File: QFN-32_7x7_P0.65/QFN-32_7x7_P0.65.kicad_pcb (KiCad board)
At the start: 2 copper layers, 25.4 x 45.7 mm, 6 parts, among them J101 Conn_01x26, J102 Conn_01x26, J103 Conn_01x26, J104 Conn_01x26, U101 QFN-48

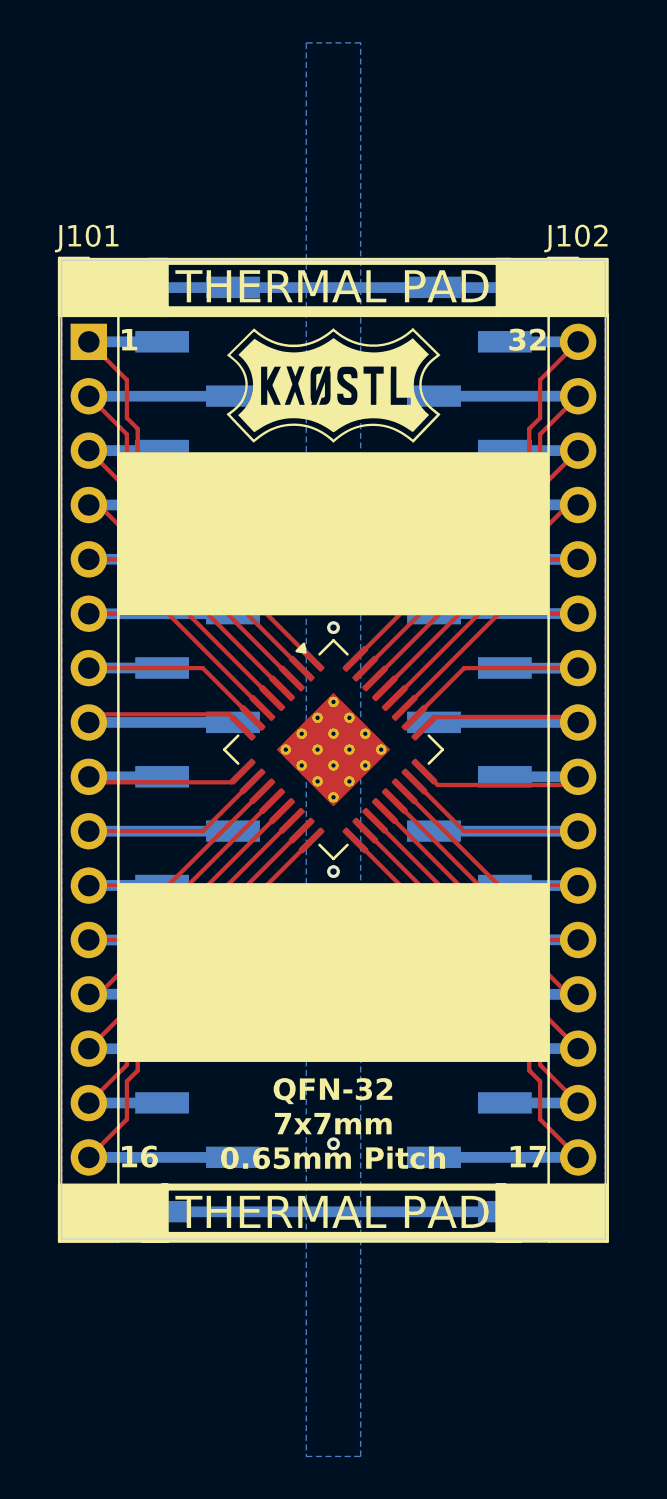
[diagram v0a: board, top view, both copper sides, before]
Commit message: Created SMDIP-16, QFP-48, QFP-32, QFN-80, QFN-68, QFN-64, QFN-60, QFN-56, QFN-48, QFN-36, QFN-28, QFN-20, QFP-32, QFP-48
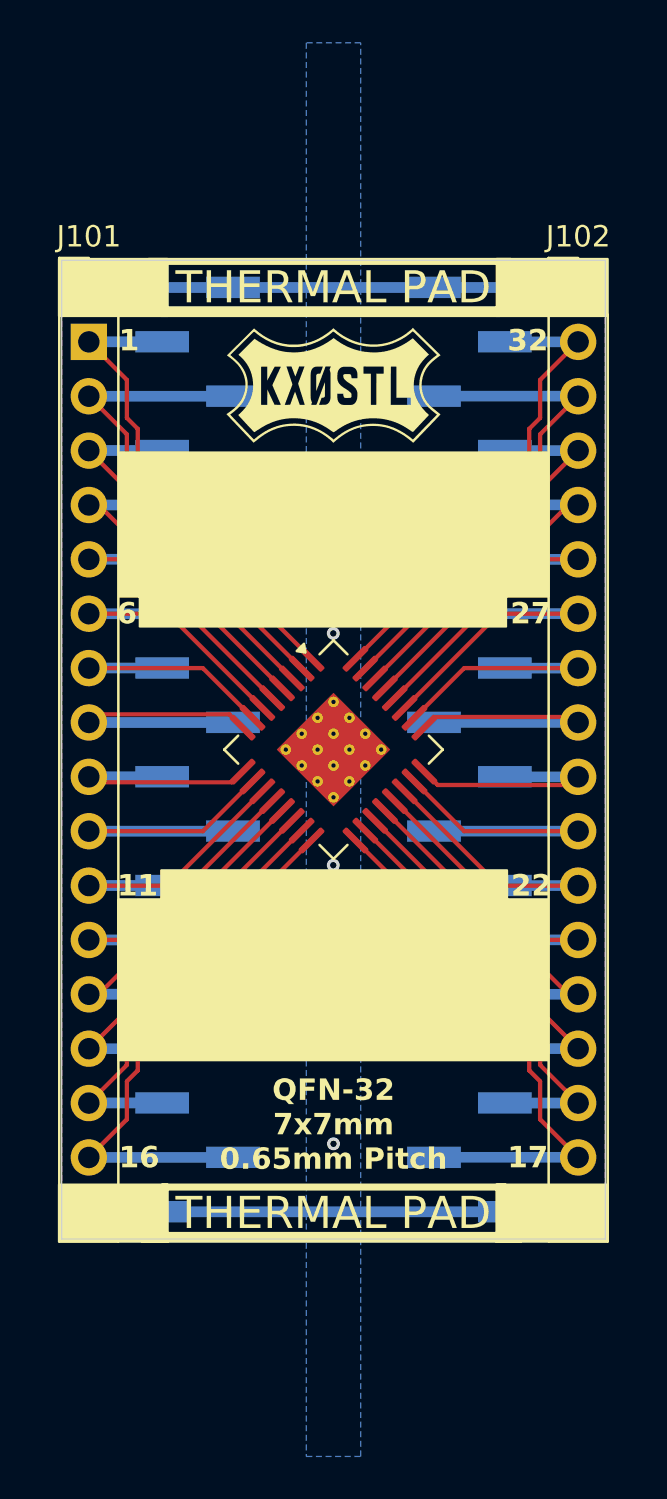
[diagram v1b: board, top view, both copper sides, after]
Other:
- board text added: "11"
- board text added: "22"
- board text added: "27"
- board text added: "6"
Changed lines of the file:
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@@
+	)
+	(gr_rect
+		(start 129.377 108.1456)
+		(end 146.493 114.9)
+		(stroke
+			(width 0.1)
+			(type solid)
+		)
+		(fill yes)
+		(layer "F.SilkS")
 	)
 	(gr_rect
@@
 	)
 	(gr_rect
+		(start 130.382 126.2856)
+		(end 146.538 128.89)
+		(stroke
+			(width 0.1)
+			(type solid)
+		)
+		(fill yes)
+		(layer "F.SilkS")
+	)
+	(gr_rect
 		(start 129.7855 97.726375)
 		(end 146.72725 97.954975)
+		(stroke
+			(width 0.1)
+			(type solid)
+		)
+		(fill yes)
+		(layer "F.SilkS")
+	)
+	(gr_rect
+		(start 128.374 127.66)
+		(end 148.43 134.271)
 		(stroke
 			(width 0.1)
@@
 	)
 	(gr_rect
-		(start 128.36935 106.807)
-		(end 148.43535 114.3254)
-		(stroke
-			(width 0.1)
-			(type solid)
-		)
-		(fill yes)
-		(layer "F.SilkS")
-	)
-	(gr_rect
 		(start 129.48075 143.2306)
 		(end 147.1845 143.637)
@@
 	)
 	(gr_rect
-		(start 128.397 126.9365)
-		(end 148.463 135.1915)
+		(start 125.603 97.726375)
+		(end 130.683 100.393625)
 		(stroke
 			(width 0.1)
@@
 	)
 	(gr_rect
-		(start 125.603 97.726375)
-		(end 130.683 100.393625)
+		(start 128.374 127.66)
+		(end 148.44 135.161)
+		(stroke
+			(width 0.1)
+			(type solid)
+		)
+		(fill yes)
+		(layer "F.SilkS")
+	)
+	(gr_rect
+		(start 128.40935 106.767)
+		(end 148.47535 113.5014)
 		(stroke
 			(width 0.1)
@@
 		)
 	)
+	(gr_text "22"
+		(at 148.63 127 0)
+		(layer "F.SilkS" knockout)
+		(effects
+			(font
+				(size 1 1)
+				(thickness 0.2)
+				(bold yes)
+			)
+			(justify right)
+		)
+	)
 	(gr_text "17"
 		(at 148.463 139.7 0)
 		(layer "F.SilkS")
+		(effects
+			(font
+				(size 1 1)
+				(thickness 0.2)
+				(bold yes)
+			)
+			(justify right)
+		)
+	)
+	(gr_text "27"
+		(at 148.6 114.29 0)
+		(layer "F.SilkS" knockout)
 		(effects
 			(font
@@
 		)
 	)
+	(gr_text "11"
+		(at 128.32 127 0)
+		(layer "F.SilkS" knockout)
+		(effects
+			(font
+				(size 1 1)
+				(thickness 0.2)
+				(bold yes)
+			)
+			(justify left)
+		)
+	)
 	(gr_text "THERMAL PAD"
 		(at 138.4215 99.06 0)
@@
 		)
 	)
-	(gr_text "1"
-		(at 128.397 101.536375 0)
-		(layer "F.SilkS")
+	(gr_text "6"
+		(at 128.3 114.29 0)
+		(layer "F.SilkS" knockout)
 		(effects
 			(font
@@
 		)
 	)
-	(gr_text "16"
-		(at 128.397 139.7 0)
+	(gr_text "1"
+		(at 128.397 101.536375 0)
 		(layer "F.SilkS")
 		(effects
@@
 		)
 	)
+	(gr_text "16"
+		(at 128.397 139.7 0)
+		(layer "F.SilkS")
+		(effects
+			(font
+				(size 1 1)
+				(thickness 0.2)
+				(bold yes)
+			)
+			(justify left)
+		)
+	)
 	(segment
 		(start 146.157216 114.301642)
@@
 	)
 	(via
-		(at 138.43 114.951)
+		(at 138.42 115.22)
 		(size 0.6)
 		(drill 0.3)
@@
 	)
 	(via
-		(at 138.43 126.349)
+		(at 138.42 126.05)
 		(size 0.6)
 		(drill 0.3)
